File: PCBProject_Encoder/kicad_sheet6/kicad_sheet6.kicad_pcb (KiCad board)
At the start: 4 copper layers, 84.8 x 83.7 mm, 71 parts, among them J1 L77HDE15SD1CH4RHNVGA, U1 DS3486M, U2 DS3486M, U3 SN74HC365D

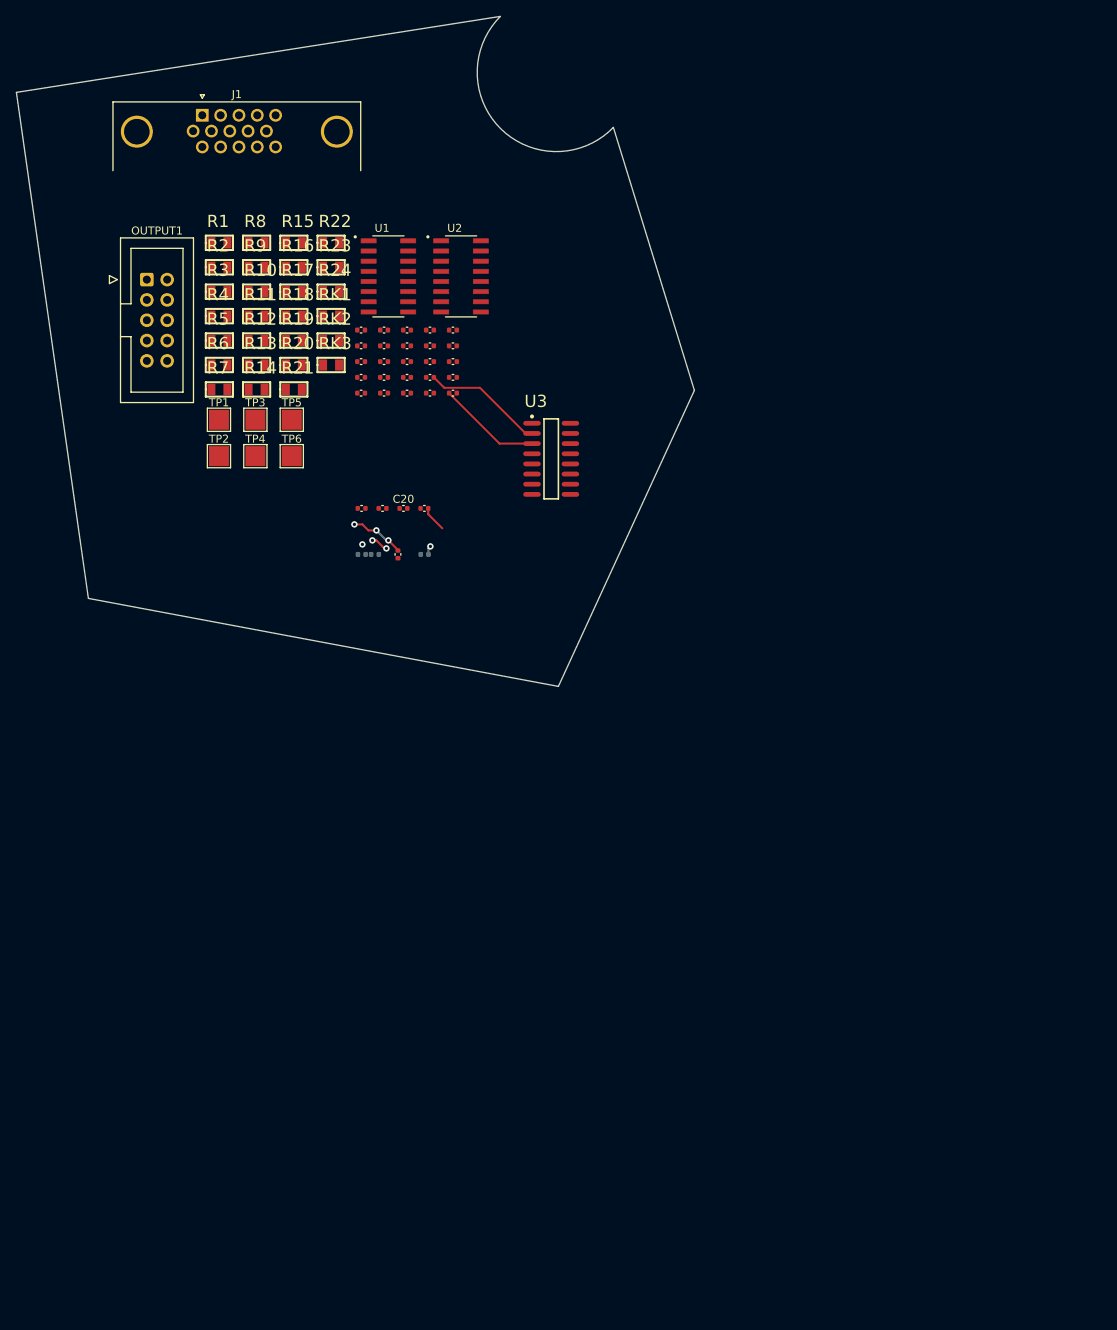
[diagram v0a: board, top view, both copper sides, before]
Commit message: add sheet6 encoder board provided by wang, qian
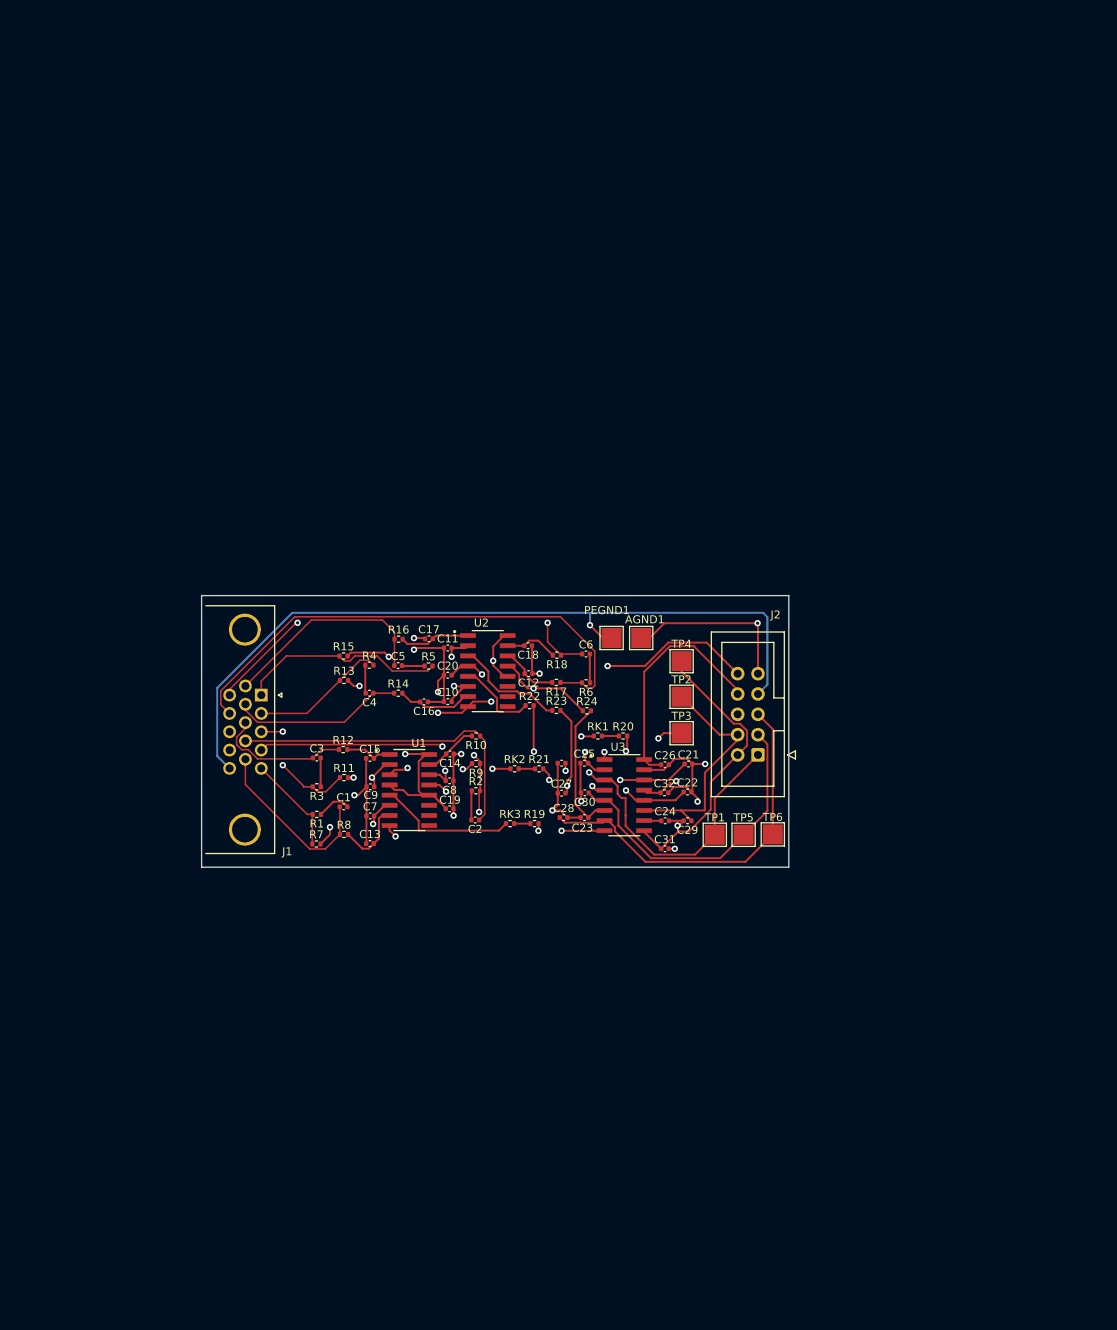
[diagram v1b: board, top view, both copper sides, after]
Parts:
- removed OUTPUT1: HIF3FC-10PA-2.54DSA, Connector_IDC:IDC-Header_2x05_P2.54mm_Vertical
- added AGND1: IV黄色测试点, TestPoint:TestPoint_Pad_2.5x2.5mm, F.Cu at (113.6, 97.2)
- added J2: HIF3FC-10PA-2.54DSA, Connector_IDC:IDC-Header_2x05_P2.54mm_Vertical, F.Cu at (128.2, 111.8)
- added PEGND1: IV黄色测试点, TestPoint:TestPoint_Pad_2.5x2.5mm, F.Cu at (109.9, 97.2)
- C21, C28, C7: moved to F.Cu
- R1, R10, R11, R12, R13, R14, R15, R16, R17, R18, R19, R2, R20, R21, R22, R23, R24, R3, R4, R5, R6, R7, R8, R9, RK1, RK2, RK3: footprint 1mmlab_footprint:0805 -> Resistor_SMD:R_0402_1005Metric
- U1, U2: footprint my-kicad-library:SOIC127P600X175-16N -> mylib_pcb:SOIC127P600X175-16N
- U3: footprint 1mmlab_footprint:D016_N -> mylib_pcb:SOIC127P600X175-16N
- moved TP1 80.8 mm to (122.8, 121.8)
- moved TP5 76.7 mm to (126.4, 121.8)
- moved TP6 76.5 mm to (130.1, 121.8)
- moved R8 74.8 mm to (76.5, 121.8)
- moved R2 72.9 mm to (92.9, 116.3)
- moved J1 72.9 mm to (66.1, 104.3), turned to -90 degrees
- moved R1 72.5 mm to (73.0, 119.2), turned to 180 degrees
- moved C29 68.0 mm to (119.4, 120.0), turned to 180 degrees
- moved R9 67.8 mm to (93.0, 112.9), turned to 180 degrees
- moved R19 67.5 mm to (100.3, 120.4)
- moved C31 66.4 mm to (116.6, 123.5)
- moved TP3 66.1 mm to (118.7, 109.1)
- moved C22 66.1 mm to (119.4, 116.5)
- moved TP2 65.2 mm to (118.7, 104.5)
- moved C24 64.5 mm to (116.6, 120.0)
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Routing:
- net AGND: track 1.10 -> 263.1 mm, vias 1 -> 19
- net D+5V: track 0.00 -> 121.1 mm, vias 0 -> 4
- net PE_GND: track 0.00 -> 98.6 mm, vias 0 -> 1
- net /HALL_W+: track 0.00 -> 64.7 mm
- net /HALL_W-: track 0.00 -> 51.4 mm, vias 0 -> 2
- net /QEP1_HALL_W: track 0.00 -> 47.3 mm
- net /ENCB-: track 0.00 -> 41.1 mm
- net /QEP1_HALL_V: track 0.00 -> 39.3 mm
- net /MQEP1A: track 0.00 -> 35.7 mm
- net /ENCB+: track 0.00 -> 34.9 mm, vias 0 -> 3
- net /MQEP1B: track 0.00 -> 29.6 mm
- net VDD: track 0.00 -> 29.3 mm
- net /QEP1_HALL_U: track 13.0 -> 39.9 mm, vias 0 -> 2
- net /HALL_V-: track 0.00 -> 26.9 mm
- net Net-(U1-OUT_B): track 0.00 -> 26.3 mm, vias 0 -> 2
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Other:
- board size 84.8 x 83.7 mm -> 73.4 x 33.9 mm

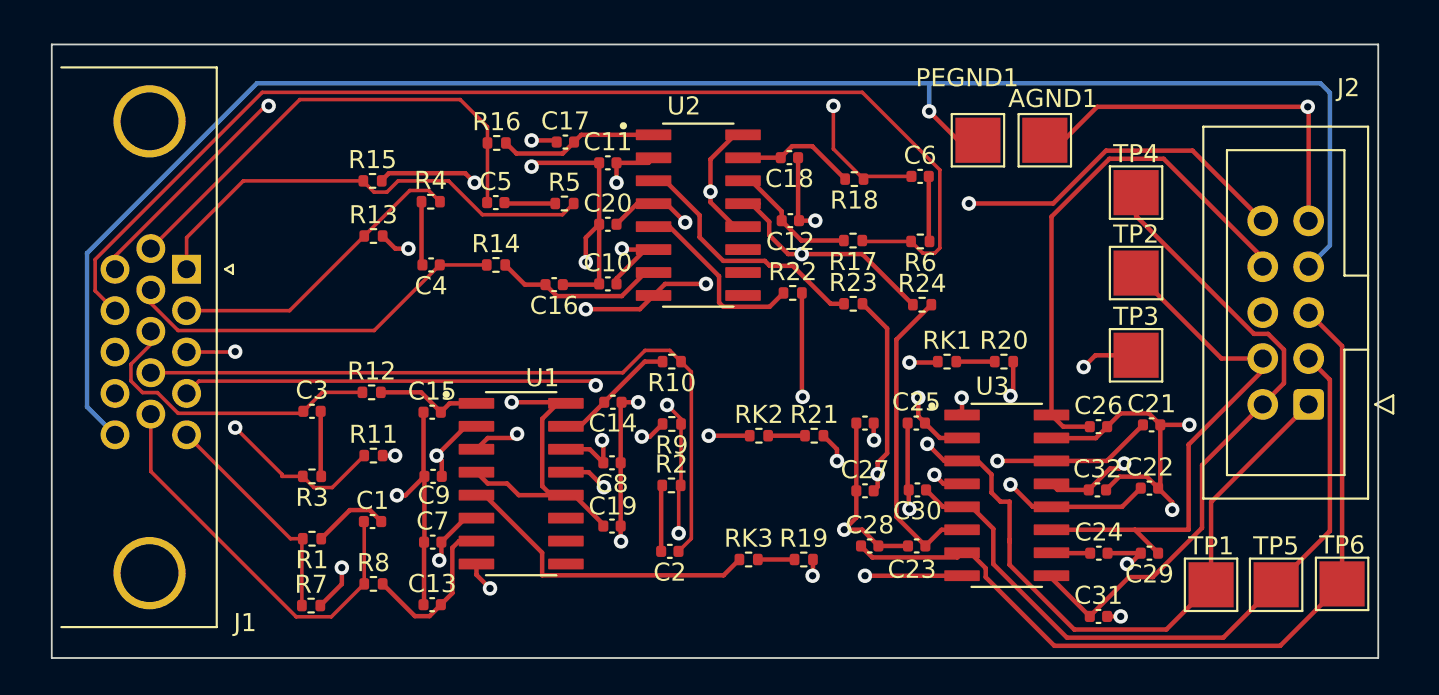
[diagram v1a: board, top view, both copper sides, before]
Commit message: alter encoder, making it better.
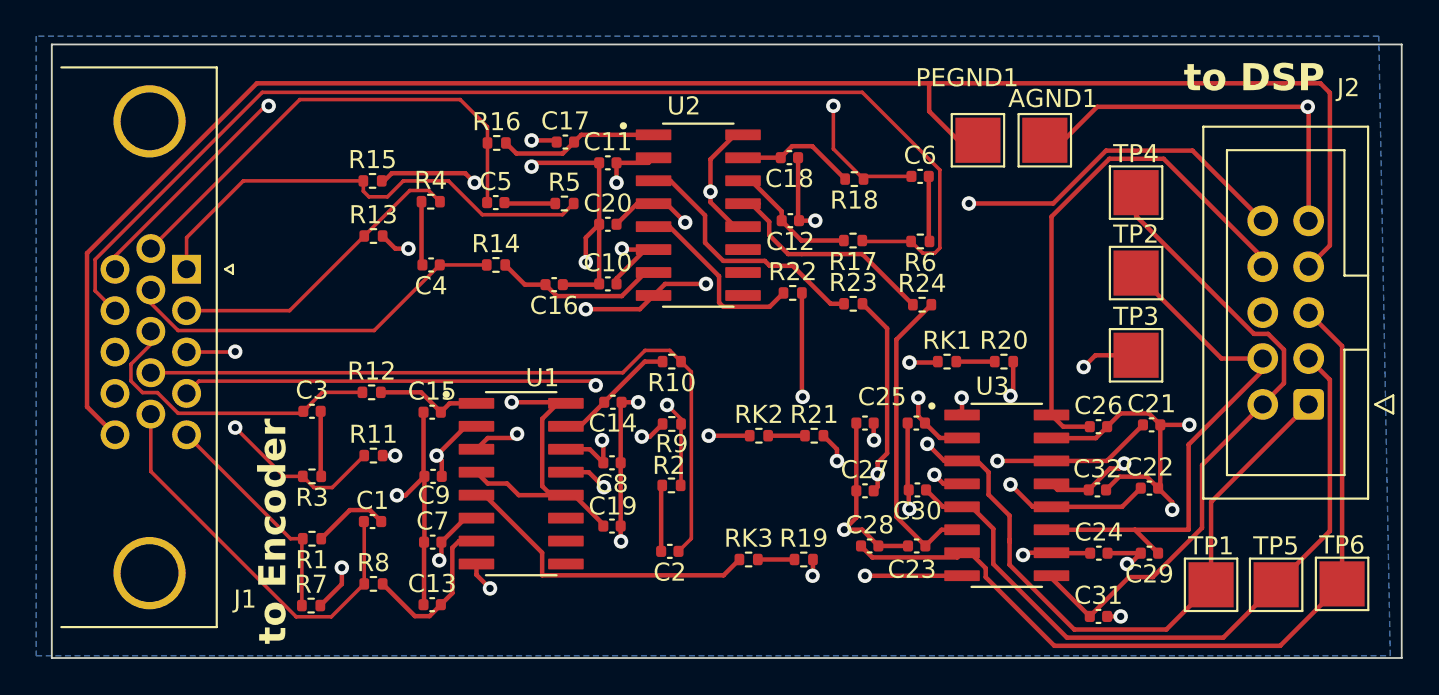
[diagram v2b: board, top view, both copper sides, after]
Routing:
- net /ENCB+: track 34.9 -> 32.4 mm, vias 3 -> 2
- net Net-(U3-4A): track 18.1 -> 19.3 mm, vias 1 -> 2
- net /HALL_V+: track 26.0 -> 26.6 mm
- net PE_GND: vias 1 -> 0
- net Net-(U2-OUT_B): vias 1 -> 0
- added copper zone on B.Cu, net AGND
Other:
- board size 73.4 x 33.9 mm -> 74.7 x 33.9 mm
- board text added: "to DSP"
- board text added: "to Encoder"

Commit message: 重新布线+原图备份x1
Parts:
- added AGND1: IV黄色测试点, TestPoint:TestPoint_Pad_2.5x2.5mm, F.Cu at (110.9, 153.1)
- added C1: 103, Capacitor_SMD:C_0805_2012Metric, F.Cu at (73.7, 174.2)
- added C10: 102, Capacitor_SMD:C_0805_2012Metric, F.Cu at (86.7, 161.0)
- added C11: 102, Capacitor_SMD:C_0805_2012Metric, F.Cu at (86.7, 154.3)
- added C12: 102, Capacitor_SMD:C_0805_2012Metric, F.Cu at (96.8, 157.5)
- added C13: 102, Capacitor_SMD:C_0805_2012Metric, F.Cu at (77.0, 178.8)
- added C14: 102, Capacitor_SMD:C_0805_2012Metric, F.Cu at (87.0, 167.6)
- added C15: 102, Capacitor_SMD:C_0805_2012Metric, F.Cu at (77.0, 168.1)
- added C16: 102, Capacitor_SMD:C_0805_2012Metric, F.Cu at (83.8, 161.0)
- added C17: 102, Capacitor_SMD:C_0805_2012Metric, F.Cu at (84.4, 153.2)
- added C18: 102, Capacitor_SMD:C_0805_2012Metric, F.Cu at (96.8, 154.0)
- added C19: 104, Capacitor_SMD:C_0805_2012Metric, F.Cu at (87.0, 174.4)
- added C2: 103, Capacitor_SMD:C_0805_2012Metric, F.Cu at (90.2, 175.8)
- added C20: 104, Capacitor_SMD:C_0805_2012Metric, F.Cu at (86.7, 157.7)
- added C21: 101, Capacitor_SMD:C_0805_2012Metric, F.Cu at (116.8, 168.8)
- added C22: 101, Capacitor_SMD:C_0805_2012Metric, F.Cu at (116.7, 172.3)
- added C23: 101, Capacitor_SMD:C_0805_2012Metric, F.Cu at (103.8, 175.5)
- added C24: 101, Capacitor_SMD:C_0805_2012Metric, F.Cu at (113.9, 175.9)
- added C25: 101, Capacitor_SMD:C_0805_2012Metric, F.Cu at (103.8, 168.7)
- added C26: 104, Capacitor_SMD:C_0805_2012Metric, F.Cu at (113.9, 168.9)
- added C27: 101, Capacitor_SMD:C_0805_2012Metric, F.Cu at (101.0, 172.4)
- added C28: 102, Capacitor_SMD:C_0805_2012Metric, F.Cu at (101.2, 175.5)
- added C29: 102, Capacitor_SMD:C_0805_2012Metric, F.Cu at (116.7, 175.9)
- added C3: 103, Capacitor_SMD:C_0805_2012Metric, F.Cu at (70.3, 168.1)
- added C30: 102, Capacitor_SMD:C_0805_2012Metric, F.Cu at (103.8, 172.4)
- added C31: 102, Capacitor_SMD:C_0805_2012Metric, F.Cu at (113.9, 179.4)
- added C32: 102, Capacitor_SMD:C_0805_2012Metric, F.Cu at (113.8, 172.4)
- added C33: 102, Capacitor_SMD:C_0805_2012Metric, F.Cu at (101.0, 168.7)
- added C4: 103, Capacitor_SMD:C_0805_2012Metric, F.Cu at (76.9, 160.0)
- added C5: 103, Capacitor_SMD:C_0805_2012Metric, F.Cu at (80.5, 156.5)
- added C6: 103, Capacitor_SMD:C_0805_2012Metric, F.Cu at (104.0, 155.1)
- added C7: 102, Capacitor_SMD:C_0805_2012Metric, F.Cu at (77.0, 175.3)
- added C8: 102, Capacitor_SMD:C_0805_2012Metric, F.Cu at (87.0, 170.9)
- added C9: 102, Capacitor_SMD:C_0805_2012Metric, F.Cu at (77.0, 171.7)
- added J2: HIF3FC-10PA-2.54DSA, Connector_IDC:IDC-Header_2x05_P2.54mm_Vertical, F.Cu at (125.5, 167.7)
- added PEGND1: IV黄色测试点, TestPoint:TestPoint_Pad_2.5x2.5mm, F.Cu at (107.2, 153.1)
- added R1: 241, Resistor_SMD:R_0805_2012Metric, F.Cu at (70.3, 175.1)
- added R10: 1001R, Resistor_SMD:R_0805_2012Metric, F.Cu at (90.3, 165.3)
- added R11: 1001R, Resistor_SMD:R_0805_2012Metric, F.Cu at (73.8, 170.5)
- added R12: 1001R, Resistor_SMD:R_0805_2012Metric, F.Cu at (73.7, 167.0)
- added R13: 1001R, Resistor_SMD:R_0805_2012Metric, F.Cu at (73.8, 158.3)
- added R14: 1001R, Resistor_SMD:R_0805_2012Metric, F.Cu at (80.5, 160.0)
- added R15: 1001R, Resistor_SMD:R_0805_2012Metric, F.Cu at (73.7, 155.3)
- added R16: 1001R, Resistor_SMD:R_0805_2012Metric, F.Cu at (80.6, 153.2)
- added R17: 1001R, Resistor_SMD:R_0805_2012Metric, F.Cu at (100.3, 158.6)
- added R18: 1001R, Resistor_SMD:R_0805_2012Metric, F.Cu at (100.4, 155.2)
- added R19: 1K, Resistor_SMD:R_0805_2012Metric, F.Cu at (97.6, 176.2)
- added R2: 241, Resistor_SMD:R_0805_2012Metric, F.Cu at (90.2, 172.2)
- added R20: 1K, Resistor_SMD:R_0805_2012Metric, F.Cu at (108.6, 165.3)
- added R21: 1K, Resistor_SMD:R_0805_2012Metric, F.Cu at (98.1, 169.4)
- added R22: 1K, Resistor_SMD:R_0805_2012Metric, F.Cu at (97.0, 161.5)
- added R23: 1K, Resistor_SMD:R_0805_2012Metric, F.Cu at (100.3, 162.1)
- added R24: 1K, Resistor_SMD:R_0805_2012Metric, F.Cu at (104.1, 162.2)
- added R3: 241, Resistor_SMD:R_0805_2012Metric, F.Cu at (70.3, 171.7)
- added R4: 241, Resistor_SMD:R_0805_2012Metric, F.Cu at (76.9, 156.5)
- added R5: 241, Resistor_SMD:R_0805_2012Metric, F.Cu at (84.3, 156.6)
- added R6: 241, Resistor_SMD:R_0805_2012Metric, F.Cu at (104.0, 158.7)
- added R7: 1001R, Resistor_SMD:R_0805_2012Metric, F.Cu at (70.3, 178.8)
- added R8: 1001R, Resistor_SMD:R_0805_2012Metric, F.Cu at (73.8, 177.6)
- added R9: 1001R, Resistor_SMD:R_0805_2012Metric, F.Cu at (90.3, 168.8)
- added RK1: 0R, Resistor_SMD:R_0805_2012Metric, F.Cu at (105.5, 165.3)
- added RK2: 0R, Resistor_SMD:R_0805_2012Metric, F.Cu at (95.1, 169.4)
- added RK3: 0R, Resistor_SMD:R_0805_2012Metric, F.Cu at (94.5, 176.2)
- added TP1: IV黄色测试点, TestPoint:TestPoint_Pad_2.5x2.5mm, F.Cu at (120.1, 177.7)
- added TP2: IV黄色测试点, TestPoint:TestPoint_Pad_2.5x2.5mm, F.Cu at (116.0, 160.4)
- added TP3: IV黄色测试点, TestPoint:TestPoint_Pad_2.5x2.5mm, F.Cu at (116.0, 164.9)
- added TP4: IV黄色测试点, TestPoint:TestPoint_Pad_2.5x2.5mm, F.Cu at (116.0, 155.9)
- added TP5: IV黄色测试点, TestPoint:TestPoint_Pad_2.5x2.5mm, F.Cu at (123.7, 177.7)
- added TP6: IV黄色测试点, TestPoint:TestPoint_Pad_2.5x2.5mm, F.Cu at (127.3, 177.6)
- added U1: DS3486M, mylib_pcb:SOIC127P600X175-16N, F.Cu at (81.9, 172.1)
- added U2: DS3486M, mylib_pcb:SOIC127P600X175-16N, F.Cu at (91.7, 157.2)
- added U3: SN74HC365D, mylib_pcb:SOIC127P600X175-16N, F.Cu at (108.8, 172.7)
- C1, C10, C11, C12, C13, C14, C15, C16, C17, C18, C19, C2, C20, C21, C22, C23, C24, C25, C26, C27, C28, C29, C3, C30, C31, C32, C33, C4, C5, C6, C7, C8, C9: footprint Capacitor_SMD:C_0402_1005Metric -> Capacitor_SMD:C_0805_2012Metric
- J1: footprint Connector_Dsub:DSUB-15-HD_Male_Horizontal_P2.29x1.98mm_EdgePinOffset3.03mm_Housed_MountingHolesOffset4.94mm -> Connector_Dsub:DSUB-15-HD_Female_Horizontal_P2.29x1.98mm_EdgePinOffset3.03mm_Housed_MountingHolesOffset4.94mm
- R1, R10, R11, R12, R13, R14, R15, R16, R17, R18, R19, R2, R20, R21, R22, R23, R24, R3, R4, R5, R6, R7, R8, R9, RK1, RK2, RK3: footprint Resistor_SMD:R_0402_1005Metric -> Resistor_SMD:R_0805_2012Metric
- moved R5 23.5 mm to (76.2, 79.8)
- moved C5 23.5 mm to (72.4, 79.8)
- moved R15 23.5 mm to (65.6, 78.6)
- moved R4 23.5 mm to (68.8, 79.8)
- moved J1 8.81 mm to (66.2, 113.2)
- moved R13 5.02 mm to (74.7, 107.2)
- moved R16 3.47 mm to (79.8, 97.2)
- moved R14 3.22 mm to (83.9, 107.2)
- moved C4 3.15 mm to (79.5, 107.2)
- moved C17 3.02 mm to (84.0, 97.2)
- moved C16 2.84 mm to (88.4, 107.2)
- moved C20 1.58 mm to (88.5, 100.6)
- moved C10 1.58 mm to (88.5, 103.9)
- moved C11 1.54 mm to (88.5, 97.2)
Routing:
- net AGND: track 263.1 -> 500.7 mm, vias 19 -> 38
- net D+5V: track 121.1 -> 206.0 mm, vias 4 -> 8
- net /QEP1_HALL_W: track 47.3 -> 94.6 mm
- net /QEP1_HALL_U: track 39.6 -> 79.3 mm, vias 2 -> 4
- net /QEP1_HALL_V: track 39.3 -> 78.7 mm
- net PE_GND: track 98.6 -> 136.0 mm
- net /MQEP1A: track 35.7 -> 71.3 mm
- net /MQEP1B: track 29.6 -> 59.1 mm
- net VDD: track 29.3 -> 58.6 mm
- net Net-(U1-OUT_B): track 26.3 -> 52.7 mm, vias 2 -> 4
- net /MQEP1Z: track 25.4 -> 50.8 mm, vias 2 -> 4
- net Net-(U3-6A): track 19.5 -> 38.9 mm, vias 2 -> 4
- net Net-(U3-4A): track 19.3 -> 38.5 mm, vias 2 -> 4
- net /HALLW-5V: track 17.7 -> 35.3 mm
- net Net-(U1-OUT_C): track 17.5 -> 35.0 mm
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- removed copper zone on B.Cu, net AGND
- removed copper zone on In1.Cu, net AGND
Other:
- board size 74.7 x 33.9 mm -> 77.4 x 89.8 mm
